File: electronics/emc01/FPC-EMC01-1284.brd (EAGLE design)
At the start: 100 x 86.6 mm, 81 parts, among them J1 CONN-RECT-26PIN-2ROWSHROUDED, J10 ICSP, J11 CONN-RECT-16PIN-2ROW, J12 CONN-RECT-16PIN-2ROW, J13 CONN-RECT-16PIN-2ROW, J14 CONN-RECT-16PIN-2ROW, J15 CONN-RECT-16PIN-2ROW, J2 PCIE, J4 MOT-X, J5 MOT-Y, J6 MOT-Z, J7 CONN-RECT-3PINJST_PH_2MM, J8 CONN-RECT-3PINJST_PH_2MM, J9 CONN-RECT-3PINJST_PH_2MM, Q4 16Mhz, SW1 SPST_TACT-EVQQ2, U1 LM2841, U10 MCP4728, U2 A4982, U3 A4982, U4 A4982, U5 ATMEGA1284P-AU

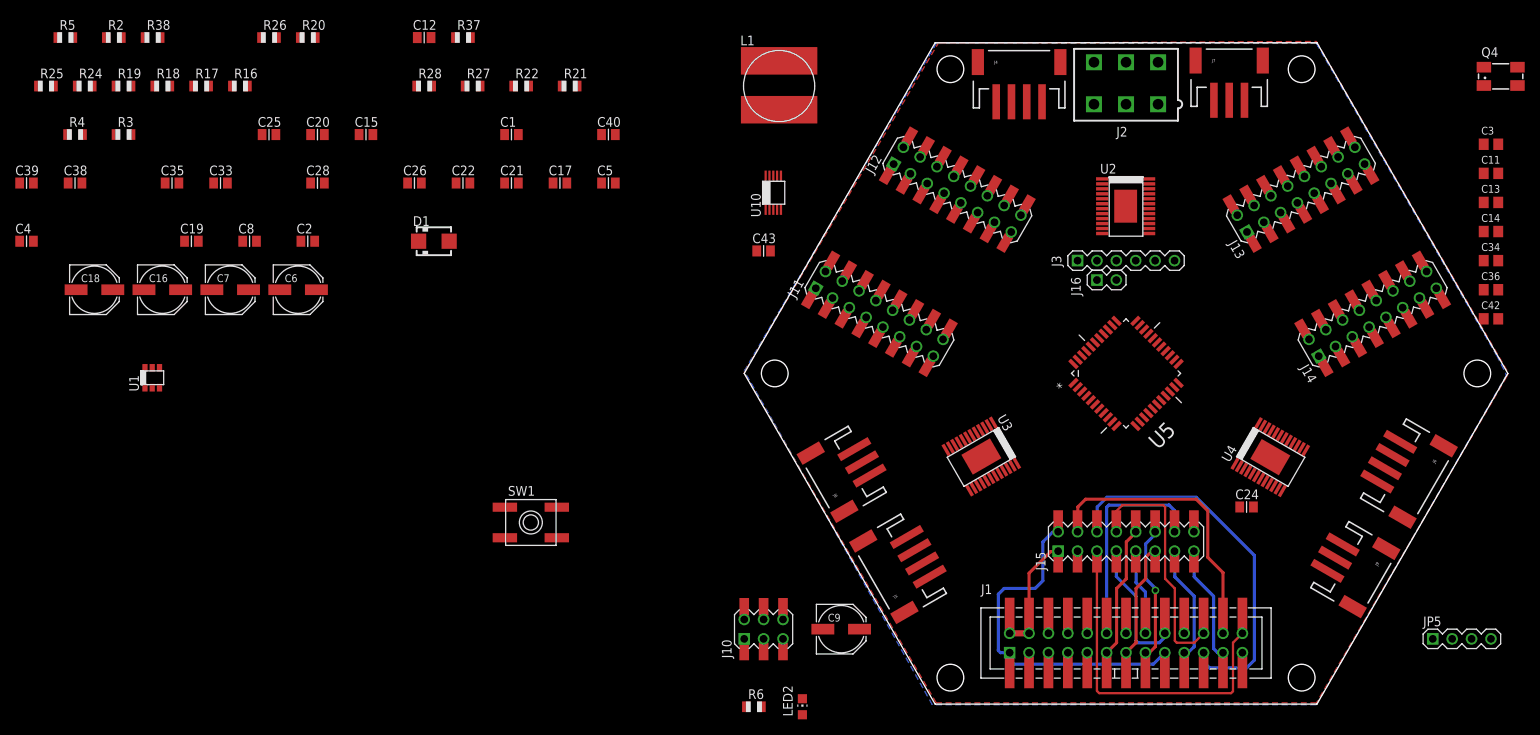
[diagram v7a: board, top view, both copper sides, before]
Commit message: Mashed everything on the board
Still trying to figure out optimal positioning for all the SMT parts.
New 5V Reg to be placed on next commit.
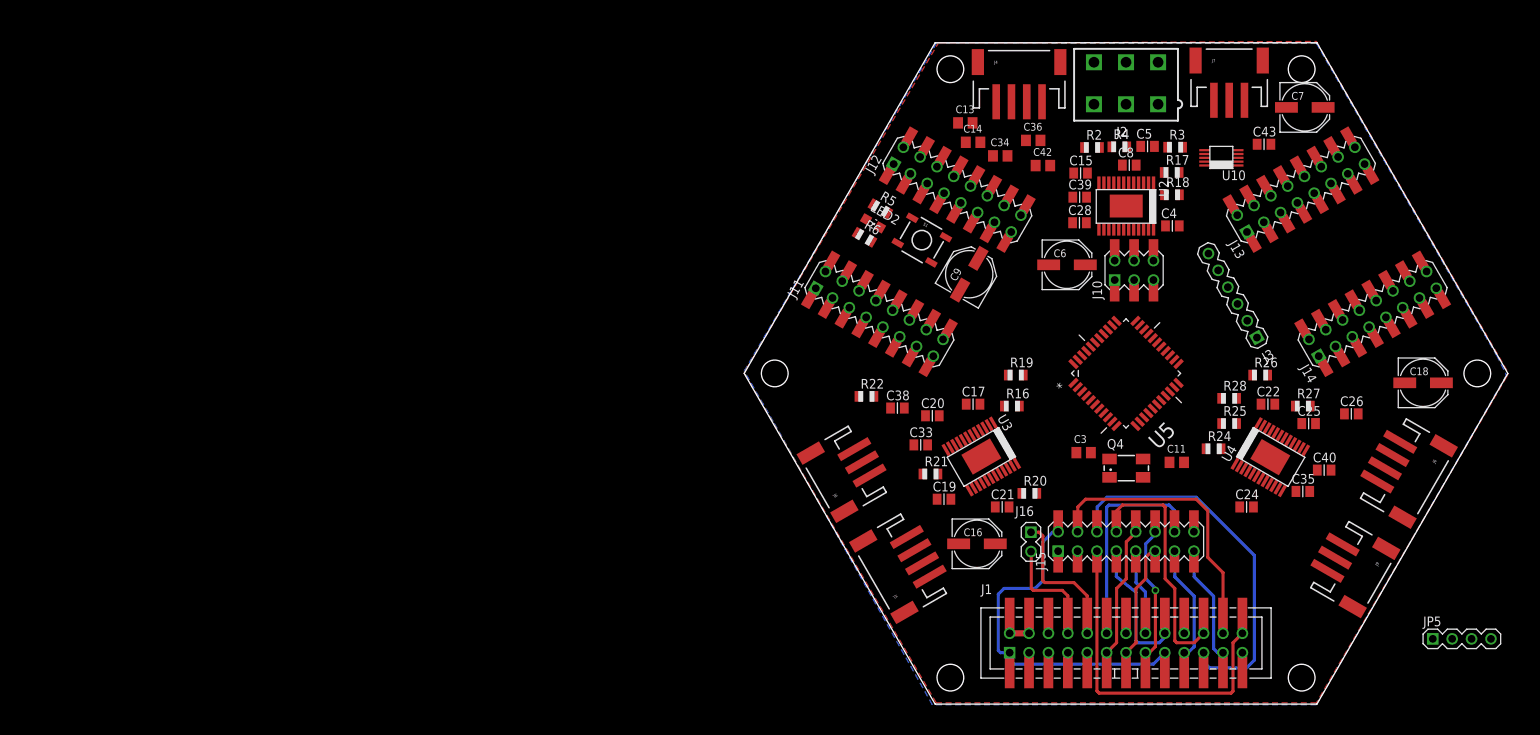
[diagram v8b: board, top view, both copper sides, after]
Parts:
- removed C1: 22uF, ipc-7351-capacitor:CAPC2012X145AN
- removed C12: 1uF, ipc-7351-capacitor:CAPC2012X145AN
- removed C2: 0.22uF, ipc-7351-capacitor:CAPC2012X145AN
- removed D1: (no value), printrbot:SMA
- removed L1: 47uH, printrbot:SDR1006
- removed R37: 5.6k, adafruit:R0805
- removed R38: 1k, adafruit:R0805
- removed SW1: SPST_TACT-EVQQ2, adafruit:EVQ-Q2
- removed U1: LM2841, printrbot:TSOT6
- added S1: (no value), SparkFun:TACTILE_SWITCH_SMD
- moved C18 174.4 mm to (88.9, 48.8)
- moved R25 161.1 mm to (63.5, 43.4)
- moved R24 155.3 mm to (61.5, 40.1)
- moved C35 153.5 mm to (73.2, 34.5)
- moved C4 150.1 mm to (56.1, 69.3)
- moved C7 142.7 mm to (73.4, 84.8)
- moved C25 141.3 mm to (73.9, 43.4)
- moved C39 137.9 mm to (43.9, 73.1)
- moved R3 137.7 mm to (56.4, 79.6)
- moved R26 137.1 mm to (67.6, 49.8)
- moved R4 136.8 mm to (49.1, 79.7)
- moved R18 133.0 mm to (56.0, 73.4)
- moved R2 128.9 mm to (45.5, 79.6)
- moved R17 127.6 mm to (56.0, 76.3)
- moved C26 126.4 mm to (79.5, 44.7)
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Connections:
- removed net N$22: R37.2, R38.1, U1.3
- removed net N$75: C2.1, D1.C, L1.P$1, U1.6
- removed net N$77: C2.2, U1.1
- net !~RESET: now also S1.3, S1.4; no longer SW1.B, SW1.B'
- net +5V: no longer C1.1, L1.P$2, R37.1
- net 12V: no longer C12.1, U1.4, U1.5
- net GND: now also S1.1, S1.2; no longer C1.2, C12.2, D1.A, R38.2, SW1.A, SW1.A', U1.2
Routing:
- net RASPI_RXD: track 0.00 -> 19.1 mm
- net RASPI_TXD: track 0.00 -> 14.9 mm
- net +5V: track 15.4 -> 2.54 mm
